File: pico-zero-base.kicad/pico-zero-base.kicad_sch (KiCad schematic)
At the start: 2 parts, among them J1 GPIO, U1 Pico

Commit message: Added reset-button
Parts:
- added SW1: SW_Push_SLIM, user:SW_PUSH_SLIM_1x4, symbol user:SW_Push_SLIM
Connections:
- net GND: now also SW1.1
- net RESET: now reaches U1.30 (RUN)
- net RESET: now also SW1.2
- no-connect marks 7 -> 6
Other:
- note added: "Reset"
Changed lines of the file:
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@@
   (junction (at 55.88 27.94) (diameter 1.016) (color 0 0 0 0)
+  )
+  (junction (at 149.86 88.265) (diameter 0) (color 0 0 0 0)
   )
   (junction (at 76.2 68.58) (diameter 1.016) (color 0 0 0 0)
@@
   (no_connect (at 86.36 125.095))
   (no_connect (at 86.36 120.015))
-  (no_connect (at 86.36 132.715))
   (no_connect (at 86.36 109.855))
   (no_connect (at 86.36 114.935))
@@
     (stroke (width 0) (type default) (color 0 0 0 0))
   )
+  (wire (pts (xy 107.95 132.715) (xy 86.36 132.715))
+    (stroke (width 0) (type default) (color 0 0 0 0))
+  )
   (wire (pts (xy 41.275 153.035) (xy 50.8 153.035))
     (stroke (width 0) (type default) (color 0 0 0 0))
@@
     (stroke (width 0) (type default) (color 0 0 0 0))
   )
+  (wire (pts (xy 149.86 90.805) (xy 149.86 88.265))
+    (stroke (width 0) (type default) (color 0 0 0 0))
+  )
   (wire (pts (xy 58.42 38.1) (xy 60.96 38.1))
     (stroke (width 0) (type solid) (color 0 0 0 0))
@@
     (stroke (width 0) (type solid) (color 0 0 0 0))
   )
+  (polyline (pts (xy 192.405 95.25) (xy 134.62 95.25))
+    (stroke (width 0) (type default) (color 0 0 0 0))
+  )
   (wire (pts (xy 41.275 132.715) (xy 50.8 132.715))
     (stroke (width 0) (type default) (color 0 0 0 0))
   )
+  (wire (pts (xy 158.115 90.805) (xy 149.86 90.805))
+    (stroke (width 0) (type default) (color 0 0 0 0))
+  )
   (wire (pts (xy 41.275 155.575) (xy 50.8 155.575))
     (stroke (width 0) (type default) (color 0 0 0 0))
@@
     (stroke (width 0) (type default) (color 0 0 0 0))
   )
+  (polyline (pts (xy 134.62 78.74) (xy 192.405 78.74))
+    (stroke (width 0) (type default) (color 0 0 0 0))
+  )
   (wire (pts (xy 76.2 68.58) (xy 73.66 68.58))
     (stroke (width 0) (type solid) (color 0 0 0 0))
@@
     (stroke (width 0) (type default) (color 0 0 0 0))
   )
+  (polyline (pts (xy 192.405 78.74) (xy 192.405 95.25))
+    (stroke (width 0) (type default) (color 0 0 0 0))
+  )
+  (wire (pts (xy 149.86 88.265) (xy 158.115 88.265))
+    (stroke (width 0) (type default) (color 0 0 0 0))
+  )
   (wire (pts (xy 31.75 66.04) (xy 60.96 66.04))
     (stroke (width 0) (type solid) (color 0 0 0 0))
@@
     (stroke (width 0) (type solid) (color 0 0 0 0))
   )
+  (wire (pts (xy 177.8 88.265) (xy 168.275 88.265))
+    (stroke (width 0) (type default) (color 0 0 0 0))
+  )
   (wire (pts (xy 41.275 120.015) (xy 50.8 120.015))
     (stroke (width 0) (type default) (color 0 0 0 0))
@@
     (stroke (width 0) (type default) (color 0 0 0 0))
   )
+  (polyline (pts (xy 134.62 78.74) (xy 134.62 95.25))
+    (stroke (width 0) (type default) (color 0 0 0 0))
+  )
   (wire (pts (xy 41.275 142.875) (xy 50.8 142.875))
     (stroke (width 0) (type default) (color 0 0 0 0))
@@
     (effects (font (size 1.27 1.27)) (justify left bottom))
   )
+  (text "Reset" (at 136.525 93.98 0)
+    (effects (font (size 1.27 1.27)) (justify left bottom))
+  )
   (label "ID_SDA" (at 31.75 60.96 0)
     (effects (font (size 1.27 1.27)) (justify left bottom))
@@
     (effects (font (size 1.27 1.27)) (justify left bottom))
   )
+  (label "RESET" (at 177.8 88.265 0)
+    (effects (font (size 1.27 1.27)) (justify left bottom))
+  )
   (label "GPIO[21]{slash}PCM.DOUT" (at 100.33 76.2 180)
     (effects (font (size 1.27 1.27)) (justify right bottom))
@@
   )
   (label "GPIO[5]" (at 107.95 140.335 0)
+    (effects (font (size 1.27 1.27)) (justify left bottom))
+  )
+  (label "RESET" (at 107.95 132.715 0)
     (effects (font (size 1.27 1.27)) (justify left bottom))
   )
@@
     (pin "1")
   )
+  (symbol (lib_id "user:SW_Push_SLIM") (at 163.195 88.265 0) (unit 1)
+    (in_bom yes) (on_board yes) (fields_autoplaced)
+    (property "Reference" "SW1" (id 0) (at 163.195 81.6442 0))
+    (property "Value" "SW_Push_SLIM" (id 1) (at 163.195 84.1811 0))
+    (property "Footprint" "user:SW_PUSH_SLIM_1x4" (id 2) (at 163.195 95.885 0)
+      (effects (font (size 1.27 1.27)) hide)
+    )
+    (property "Datasheet" "" (id 3) (at 163.195 83.185 0)
+      (effects (font (size 1.27 1.27)) hide)
+    )
+    (pin "1")
+    (pin "1")
+    (pin "2")
+  )
   (symbol (lib_id "power:GND") (at 97.79 165.1 0) (unit 1)
     (in_bom yes) (on_board yes)
@@
     (property "Footprint" "" (id 2) (at 97.79 165.1 0))
     (property "Datasheet" "" (id 3) (at 97.79 165.1 0))
+    (pin "1")
+  )
+  (symbol (lib_id "power:GND") (at 149.86 88.265 180) (unit 1)
+    (in_bom yes) (on_board yes)
+    (property "Reference" "#PWR?" (id 0) (at 149.86 81.915 0)
+      (effects (font (size 1.27 1.27)) hide)
+    )
+    (property "Value" "GND" (id 1) (at 149.7457 83.9406 0))
+    (property "Footprint" "" (id 2) (at 149.86 88.265 0))
+    (property "Datasheet" "" (id 3) (at 149.86 88.265 0))
     (pin "1")
   )
@@
       (reference "#PWR0111") (unit 1) (value "+3.3V") (footprint "")
     )
+    (path "/5405b1c2-070d-4878-91a2-8a5edbb70187"
+      (reference "#PWR?") (unit 1) (value "GND") (footprint "")
+    )
     (path "/00000000-0000-0000-0000-000059ad464a"
       (reference "J1") (unit 1) (value "GPIO") (footprint "Connector_PinSocket_2.54mm:PinSocket_2x20_P2.54mm_Vertical")
     )
+    (path "/338ef203-6f01-4f47-b338-1469df920fd2"
+      (reference "SW1") (unit 1) (value "SW_Push_SLIM") (footprint "user:SW_PUSH_SLIM_1x4")
+    )
     (path "/9fb5ec54-5948-4b9f-83f9-56bf2d8bfa53"

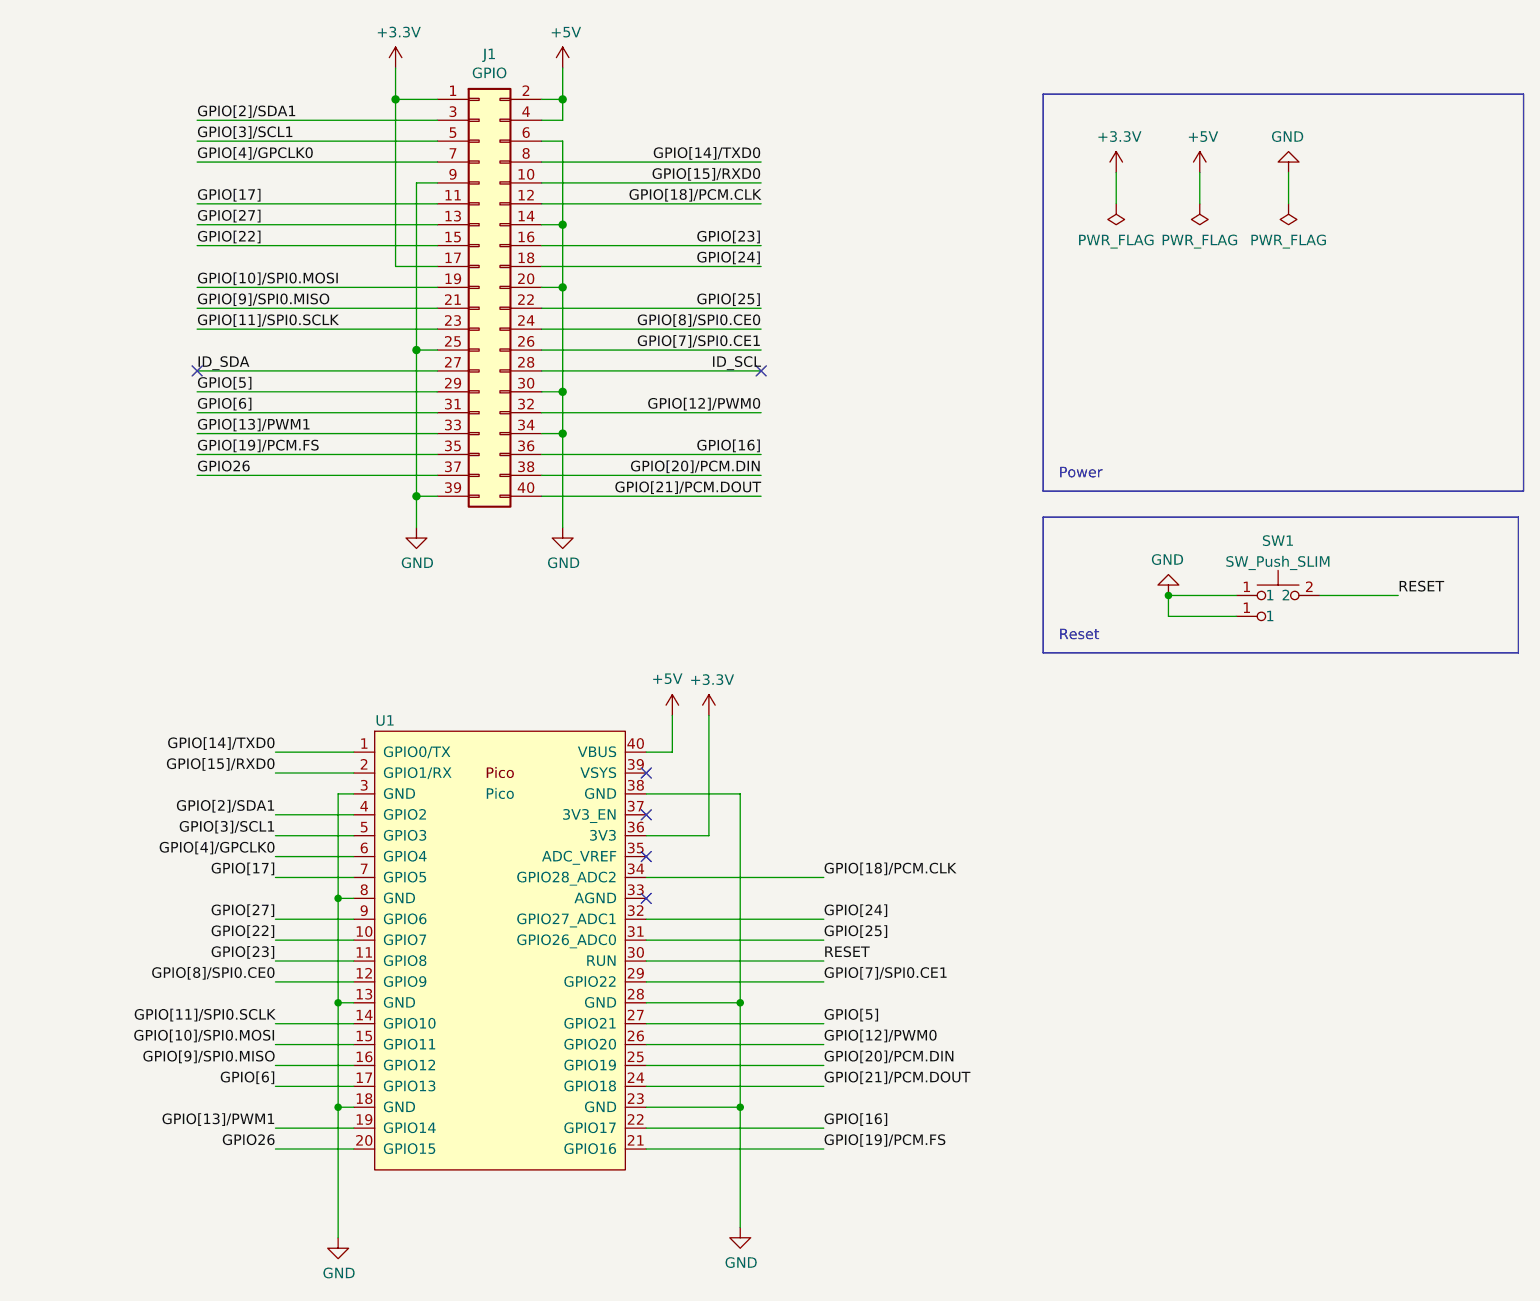
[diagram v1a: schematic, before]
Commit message: use pin-header instead of socket Rev 1.1
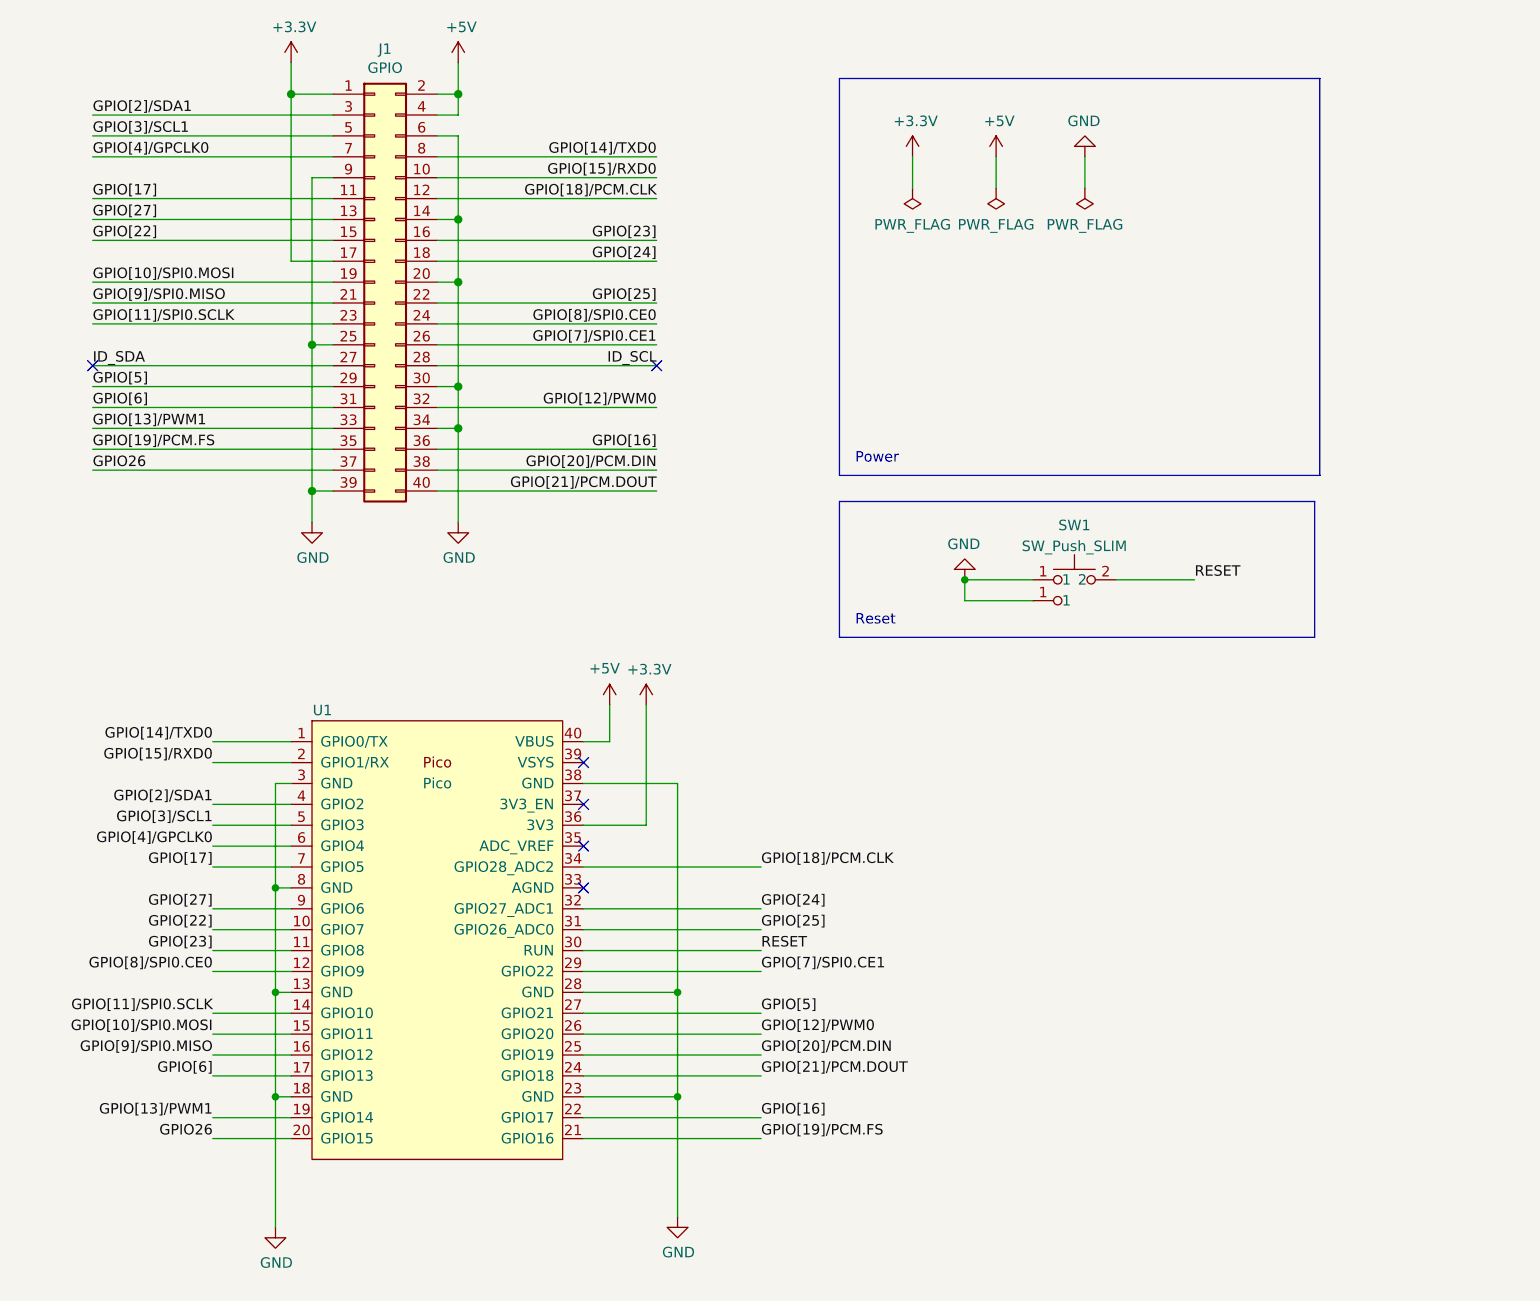
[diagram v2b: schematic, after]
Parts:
- J1: footprint Connector_PinSocket_2.54mm:PinSocket_2x20_P2.54mm_Vertical -> Connector_PinHeader_2.54mm:PinHeader_2x20_P2.54mm_Vertical
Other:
- moved on the sheet: J1, SW1, U1
